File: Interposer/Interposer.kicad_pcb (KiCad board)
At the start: 2 copper layers, 55 x 52 mm, 6 parts

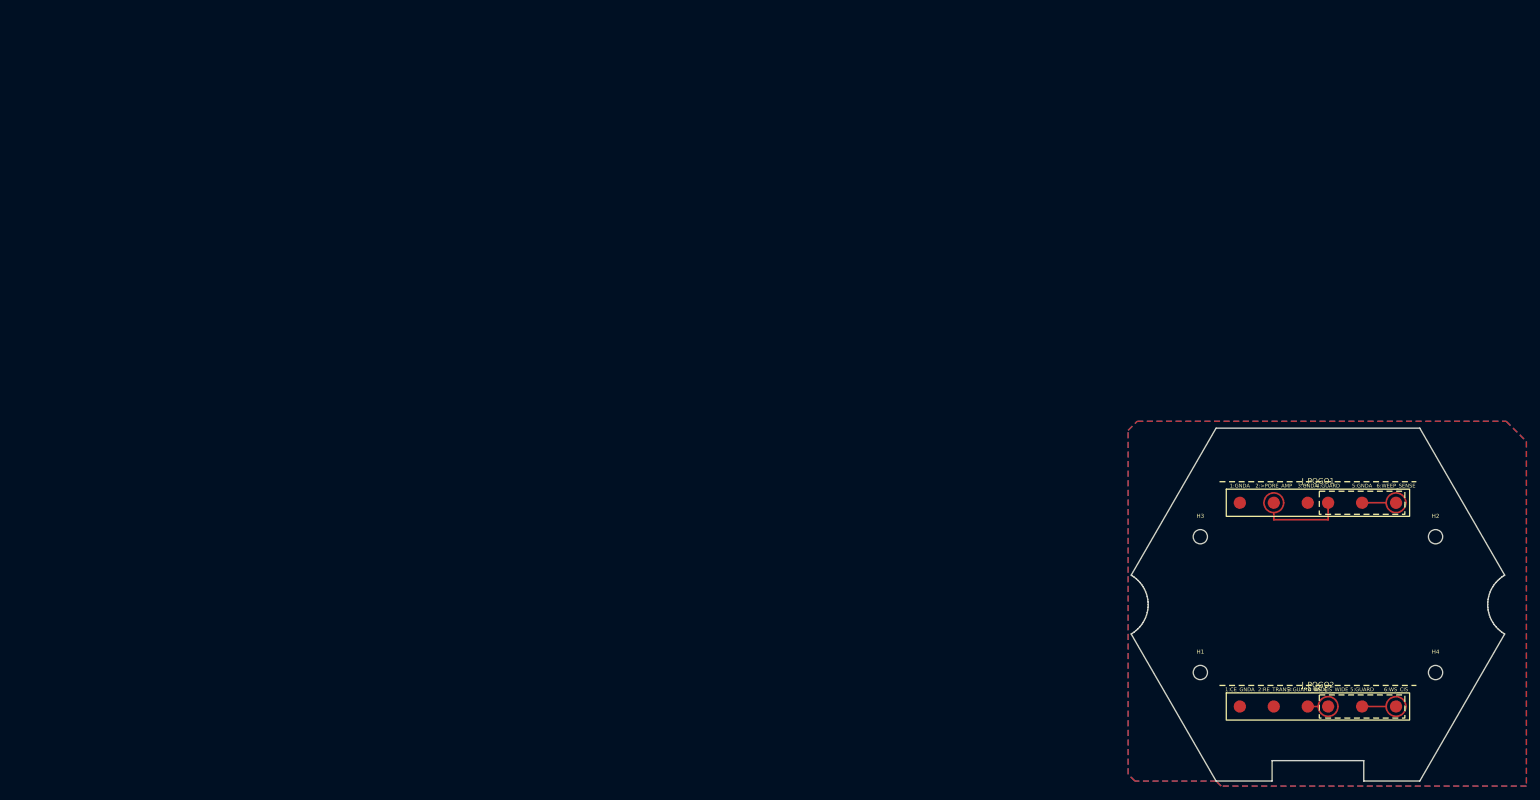
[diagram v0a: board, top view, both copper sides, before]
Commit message: feat: implement distributed 2x6 pogo pin map ($36mm span) across Bank A and Bank B
Co-authored-by: google-labs-jules[bot] <161369871+google-labs-jules[bot]@users.noreply.github.com>
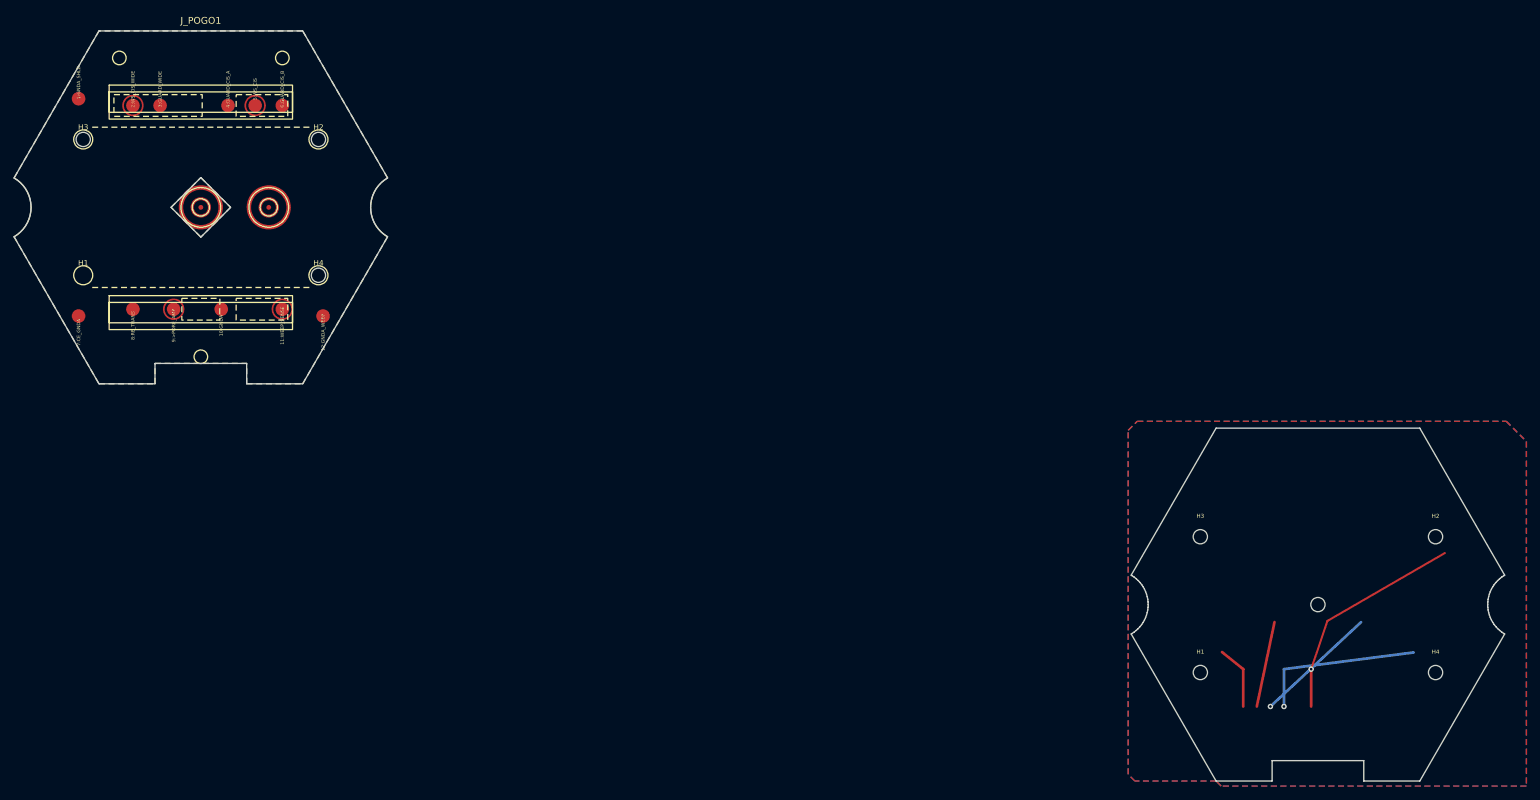
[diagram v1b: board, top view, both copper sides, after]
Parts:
- removed J_POGO2: PogoPin_Target_6Pin_Trans, footprints:PogoPin_Target_6Pin_Trans
- J_POGO1: value PogoPin_Target_6Pin_Cis -> PogoPin_Target_12Pin_Distributed; footprint footprints:PogoPin_Target_6Pin_Cis -> PogoPin_Target_12Pin_Distributed
- moved J_POGO1 170.2 mm to (0.00, 0.00)
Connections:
- J_POGO1 pad 1: GNDA -> (no net)
- J_POGO1 pad 2: >PORE_AMP -> (no net)
- J_POGO1 pad 3: GNDA -> (no net)
- J_POGO1 pad 4: GUARD -> (no net)
- J_POGO1 pad 5: GNDA -> (no net)
- J_POGO1 pad 6: WEEP_SENSE -> (no net)
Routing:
- net WEEP_SENSE: track 0.00 -> 33.0 mm, vias 0 -> 1
- net CE_GNDA: track 0.00 -> 24.8 mm, vias 0 -> 1
- net RE_TRANS: track 0.00 -> 18.2 mm, vias 0 -> 1
- net GUARD: track 15.1 -> 0.00 mm
- net WS_CIS: track 0.00 -> 12.7 mm
- net WE_POS: track 0.00 -> 9.51 mm
- net GNDA: track 3.55 -> 0.00 mm
- net GUARD_WIDE: track 1.55 -> 0.00 mm
